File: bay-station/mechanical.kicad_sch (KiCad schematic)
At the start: 4 parts

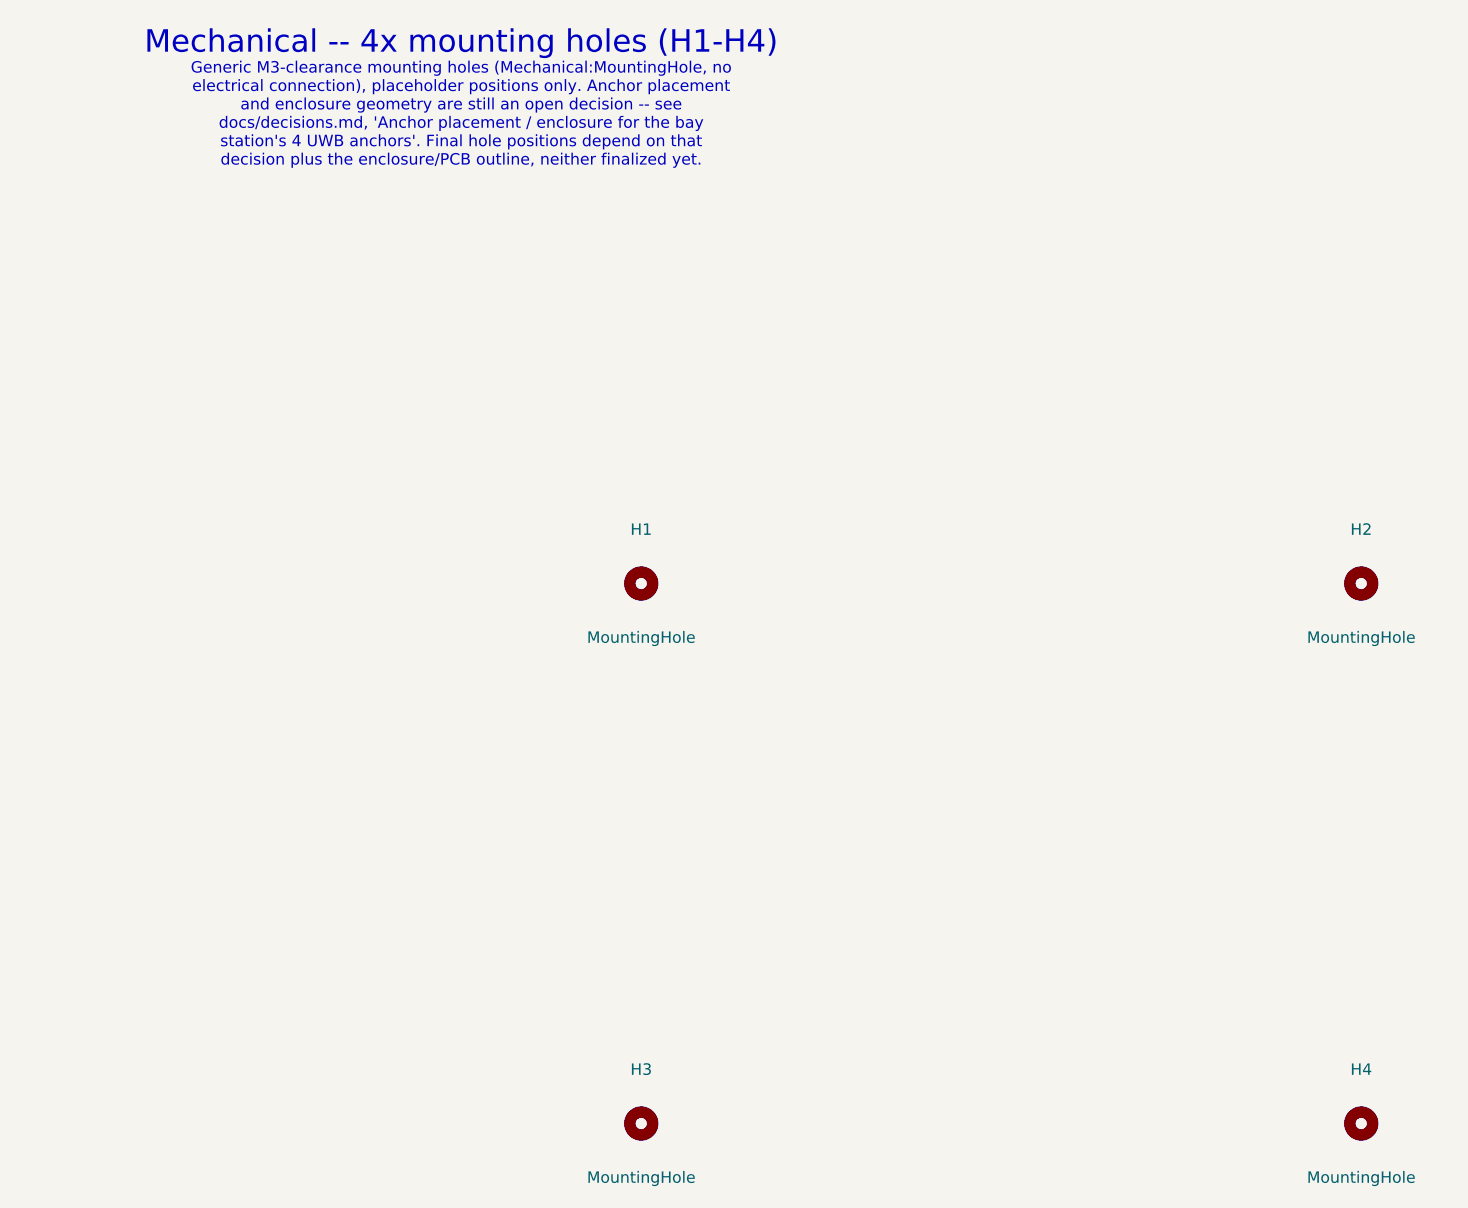
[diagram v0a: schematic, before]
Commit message: Wire up power_bms, regulation and programming_debug; tie off floating grounds
The bay station was built entirely from global labels and power symbols --
zero drawn wires on any sheet. This starts converting the power path to
explicit wiring and connects the grounds that were left floating:

- power_bms: 62 wires; 31 label justifications flipped left->right where
  the labels were mirrored. No symbols added or removed.
- regulation: 11 wires, 3 junctions, 5 GND symbols (#PWR01-05).
- programming_debug: 2 wires, 1 junction, 1 GND symbol (#PWR06).

ERC goes 518 -> 497 violations (494 -> 473 errors), entirely in
pin_not_connected (360 -> 342), power_pin_not_driven (98 -> 96) and
pin_not_driven (36 -> 35). Nothing regressed. The remaining 342
pin_not_connected are the sheets that are still label-only.

Unavoidable churn in this commit: KiCad 10 re-serialized seven sheets from
8.0 format (version 20231120) to 10.0 (20260306) on save -- clock_dist,
connectivity, gnss, indicators, programming_debug, testpoints, uwb_array.
That accounts for most of the diff; those seven have no content change
beyond it. CLAUDE.md asks that the format not be bumped as a side effect,
but it cannot be split out here: kicad-cli sch upgrade serializes
differently from the GUI and leaves ~3700 lines of residual churn, so a
format-only commit would be tidier in shape and no more honest. Four
sheets were already on 10.0 format before this commit.

Co-Authored-By: Claude Opus 5 (1M context) <noreply@anthropic.com>
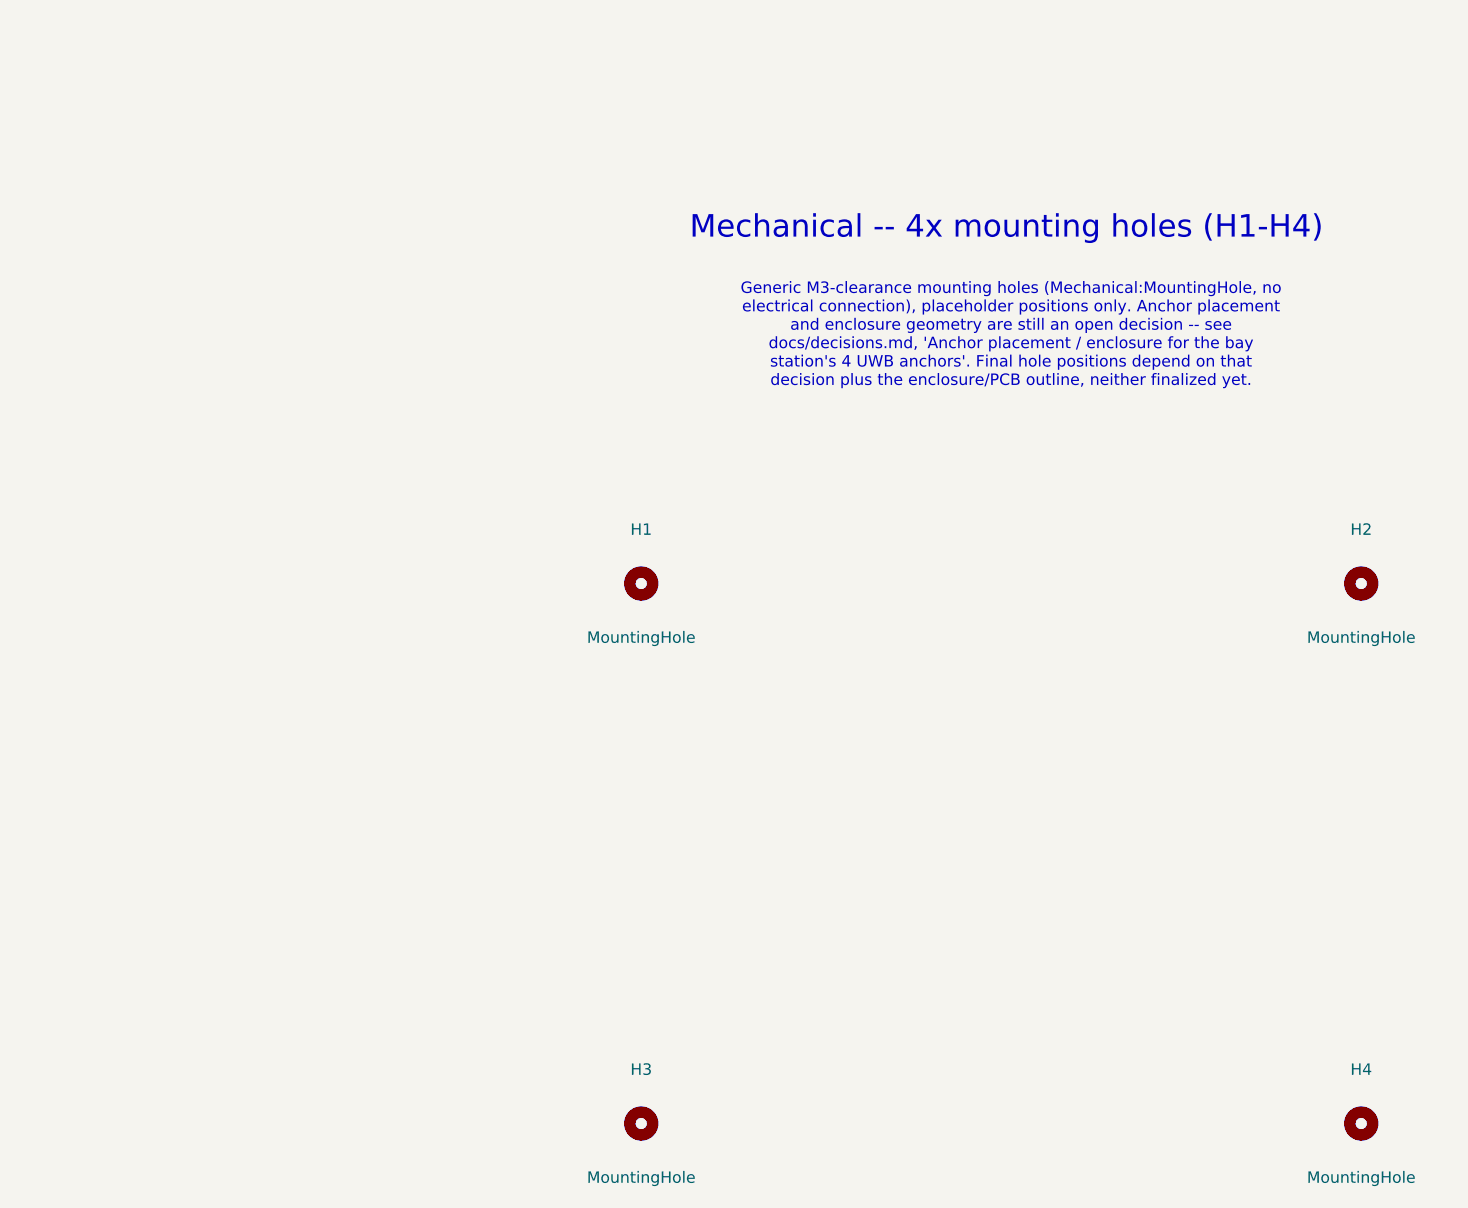
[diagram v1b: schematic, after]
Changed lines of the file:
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@@
 	)
 	(text "Mechanical -- 4x mounting holes (H1-H4)"
-		(at 40 30 0)
+		(exclude_from_sim no)
+		(at 100.584 50.546 0)
 		(effects
 			(font
@@
 	)
 	(text "Generic M3-clearance mounting holes (Mechanical:MountingHole, no\nelectrical connection), placeholder positions only. Anchor placement\nand enclosure geometry are still an open decision -- see\ndocs/decisions.md, 'Anchor placement / enclosure for the bay\nstation's 4 UWB anchors'. Final hole positions depend on that\ndecision plus the enclosure/PCB outline, neither finalized yet."
-		(at 40 38 0)
+		(exclude_from_sim no)
+		(at 101.092 62.484 0)
 		(effects
 			(font
@@
 	(symbol
 		(lib_id "Mechanical:MountingHole")
+		(at 60 150 0)
+		(unit 1)
+		(body_style 1)
+		(exclude_from_sim no)
+		(in_bom no)
+		(on_board yes)
+		(in_pos_files yes)
+		(dnp no)
+		(property "Reference" "H3"
+			(at 60 144 0)
+			(show_name no)
+			(do_not_autoplace no)
+			(effects
+				(font
+					(size 1.27 1.27)
+				)
+			)
+		)
+		(property "Value" "MountingHole"
+			(at 60 156 0)
+			(show_name no)
+			(do_not_autoplace no)
+			(effects
+				(font
+					(size 1.27 1.27)
+				)
+			)
+		)
+		(property "Footprint" "MountingHole:MountingHole_3.2mm_M3"
+			(at 60 150 0)
+			(hide yes)
+			(show_name no)
+			(do_not_autoplace no)
+			(effects
+				(font
+					(size 1.27 1.27)
+				)
+			)
+		)
+		(property "Datasheet" ""
+			(at 60 150 0)
+			(hide yes)
+			(show_name no)
+			(do_not_autoplace no)
+			(effects
+				(font
+					(size 1.27 1.27)
+				)
+			)
+		)
+		(property "Description" "Mounting Hole without connection, M3 clearance (3.2mm)"
+			(at 60 150 0)
+			(hide yes)
+			(show_name no)
+			(do_not_autoplace no)
+			(effects
+				(font
+					(size 1.27 1.27)
+				)
+			)
+		)
+		(instances
+			(project "bay-station"
+				(path "/543ba435-6cf4-448c-821e-3c5778b02e9c/adf6c49a-dc88-4f76-9bc6-0f3625bf3bc5"
+					(reference "H3")
+					(unit 1)
+				)
+			)
+		)
+	)
+	(symbol
+		(lib_id "Mechanical:MountingHole")
+		(at 140 90 0)
+		(unit 1)
+		(body_style 1)
+		(exclude_from_sim no)
+		(in_bom no)
+		(on_board yes)
+		(in_pos_files yes)
+		(dnp no)
+		(property "Reference" "H2"
+			(at 140 84 0)
+			(show_name no)
+			(do_not_autoplace no)
+			(effects
+				(font
+					(size 1.27 1.27)
+				)
+			)
+		)
+		(property "Value" "MountingHole"
+			(at 140 96 0)
+			(show_name no)
+			(do_not_autoplace no)
+			(effects
+				(font
+					(size 1.27 1.27)
+				)
+			)
+		)
+		(property "Footprint" "MountingHole:MountingHole_3.2mm_M3"
+			(at 140 90 0)
+			(hide yes)
+			(show_name no)
+			(do_not_autoplace no)
+			(effects
+				(font
+					(size 1.27 1.27)
+				)
+			)
+		)
+		(property "Datasheet" ""
+			(at 140 90 0)
+			(hide yes)
+			(show_name no)
+			(do_not_autoplace no)
+			(effects
+				(font
+					(size 1.27 1.27)
+				)
+			)
+		)
+		(property "Description" "Mounting Hole without connection, M3 clearance (3.2mm)"
+			(at 140 90 0)
+			(hide yes)
+			(show_name no)
+			(do_not_autoplace no)
+			(effects
+				(font
+					(size 1.27 1.27)
+				)
+			)
+		)
+		(instances
+			(project "bay-station"
+				(path "/543ba435-6cf4-448c-821e-3c5778b02e9c/adf6c49a-dc88-4f76-9bc6-0f3625bf3bc5"
+					(reference "H2")
+					(unit 1)
+				)
+			)
+		)
+	)
+	(symbol
+		(lib_id "Mechanical:MountingHole")
 		(at 60 90 0)
 		(unit 1)
+		(body_style 1)
 		(exclude_from_sim no)
 		(in_bom no)
@@
 	(symbol
 		(lib_id "Mechanical:MountingHole")
-		(at 140 90 0)
-		(unit 1)
-		(exclude_from_sim no)
-		(in_bom no)
-		(on_board yes)
-		(in_pos_files yes)
-		(dnp no)
-		(property "Reference" "H2"
-			(at 140 84 0)
-			(show_name no)
-			(do_not_autoplace no)
-			(effects
-				(font
-					(size 1.27 1.27)
-				)
-			)
-		)
-		(property "Value" "MountingHole"
-			(at 140 96 0)
-			(show_name no)
-			(do_not_autoplace no)
-			(effects
-				(font
-					(size 1.27 1.27)
-				)
-			)
-		)
-		(property "Footprint" "MountingHole:MountingHole_3.2mm_M3"
-			(at 140 90 0)
-			(hide yes)
-			(show_name no)
-			(do_not_autoplace no)
-			(effects
-				(font
-					(size 1.27 1.27)
-				)
-			)
-		)
-		(property "Datasheet" ""
-			(at 140 90 0)
-			(hide yes)
-			(show_name no)
-			(do_not_autoplace no)
-			(effects
-				(font
-					(size 1.27 1.27)
-				)
-			)
-		)
-		(property "Description" "Mounting Hole without connection, M3 clearance (3.2mm)"
-			(at 140 90 0)
-			(hide yes)
-			(show_name no)
-			(do_not_autoplace no)
-			(effects
-				(font
-					(size 1.27 1.27)
-				)
-			)
-		)
-		(instances
-			(project "bay-station"
-				(path "/543ba435-6cf4-448c-821e-3c5778b02e9c/adf6c49a-dc88-4f76-9bc6-0f3625bf3bc5"
-					(reference "H2")
-					(unit 1)
-				)
-			)
-		)
-	)
-	(symbol
-		(lib_id "Mechanical:MountingHole")
-		(at 60 150 0)
-		(unit 1)
-		(exclude_from_sim no)
-		(in_bom no)
-		(on_board yes)
-		(in_pos_files yes)
-		(dnp no)
-		(property "Reference" "H3"
-			(at 60 144 0)
-			(show_name no)
-			(do_not_autoplace no)
-			(effects
-				(font
-					(size 1.27 1.27)
-				)
-			)
-		)
-		(property "Value" "MountingHole"
-			(at 60 156 0)
-			(show_name no)
-			(do_not_autoplace no)
-			(effects
-				(font
-					(size 1.27 1.27)
-				)
-			)
-		)
-		(property "Footprint" "MountingHole:MountingHole_3.2mm_M3"
-			(at 60 150 0)
-			(hide yes)
-			(show_name no)
-			(do_not_autoplace no)
-			(effects
-				(font
-					(size 1.27 1.27)
-				)
-			)
-		)
-		(property "Datasheet" ""
-			(at 60 150 0)
-			(hide yes)
-			(show_name no)
-			(do_not_autoplace no)
-			(effects
-				(font
-					(size 1.27 1.27)
-				)
-			)
-		)
-		(property "Description" "Mounting Hole without connection, M3 clearance (3.2mm)"
-			(at 60 150 0)
-			(hide yes)
-			(show_name no)
-			(do_not_autoplace no)
-			(effects
-				(font
-					(size 1.27 1.27)
-				)
-			)
-		)
-		(instances
-			(project "bay-station"
-				(path "/543ba435-6cf4-448c-821e-3c5778b02e9c/adf6c49a-dc88-4f76-9bc6-0f3625bf3bc5"
-					(reference "H3")
-					(unit 1)
-				)
-			)
-		)
-	)
-	(symbol
-		(lib_id "Mechanical:MountingHole")
 		(at 140 150 0)
 		(unit 1)
-		(exclude_from_sim no)
-		(in_bom no)
+		(body_style 1)
+		(exclude_from_sim no)
+		(in_bom no)
